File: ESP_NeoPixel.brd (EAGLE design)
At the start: 25.6 x 34.1 mm, 19 parts, among them J1 CONN_08, J2 CONN_08, J3 MKDS3-2-5.00, J4 MKDS3-3-5.00, Q1 BSN20,215, U1 LMZ21700

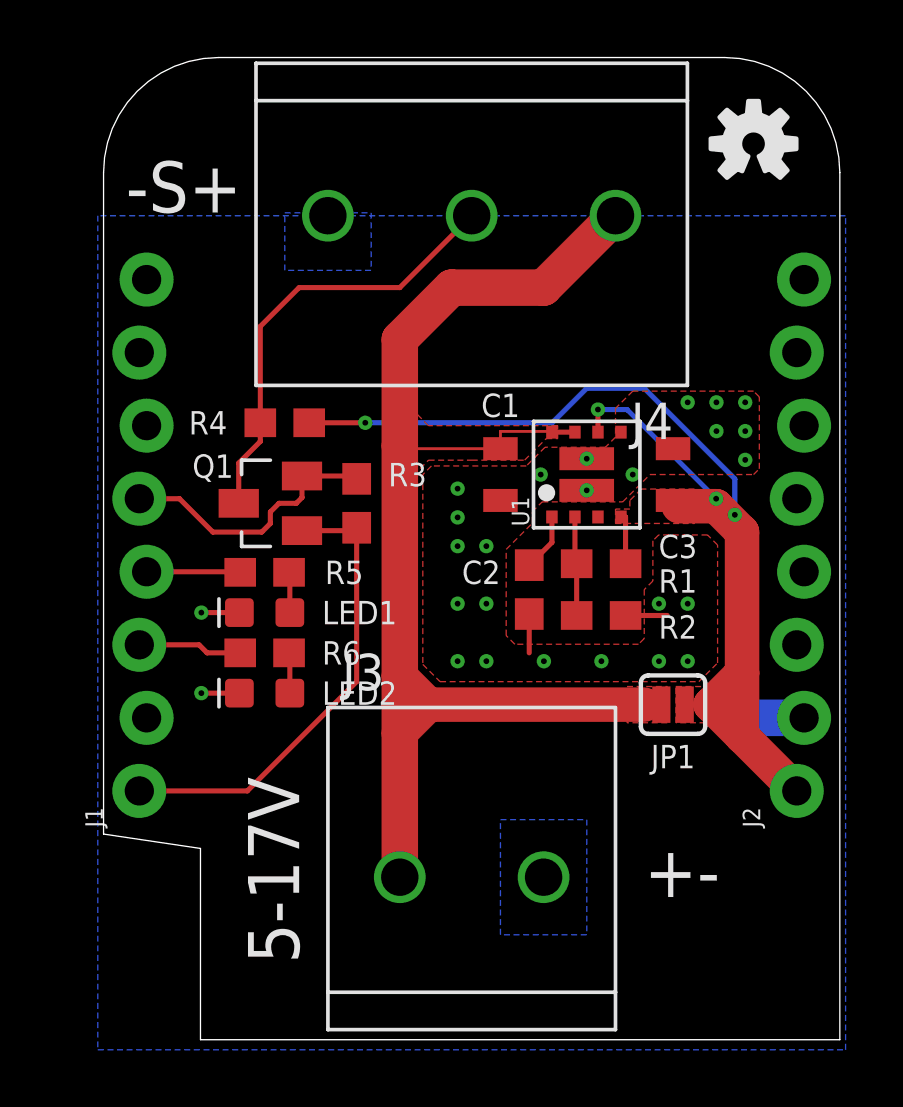
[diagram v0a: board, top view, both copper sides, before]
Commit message: added switch to D8
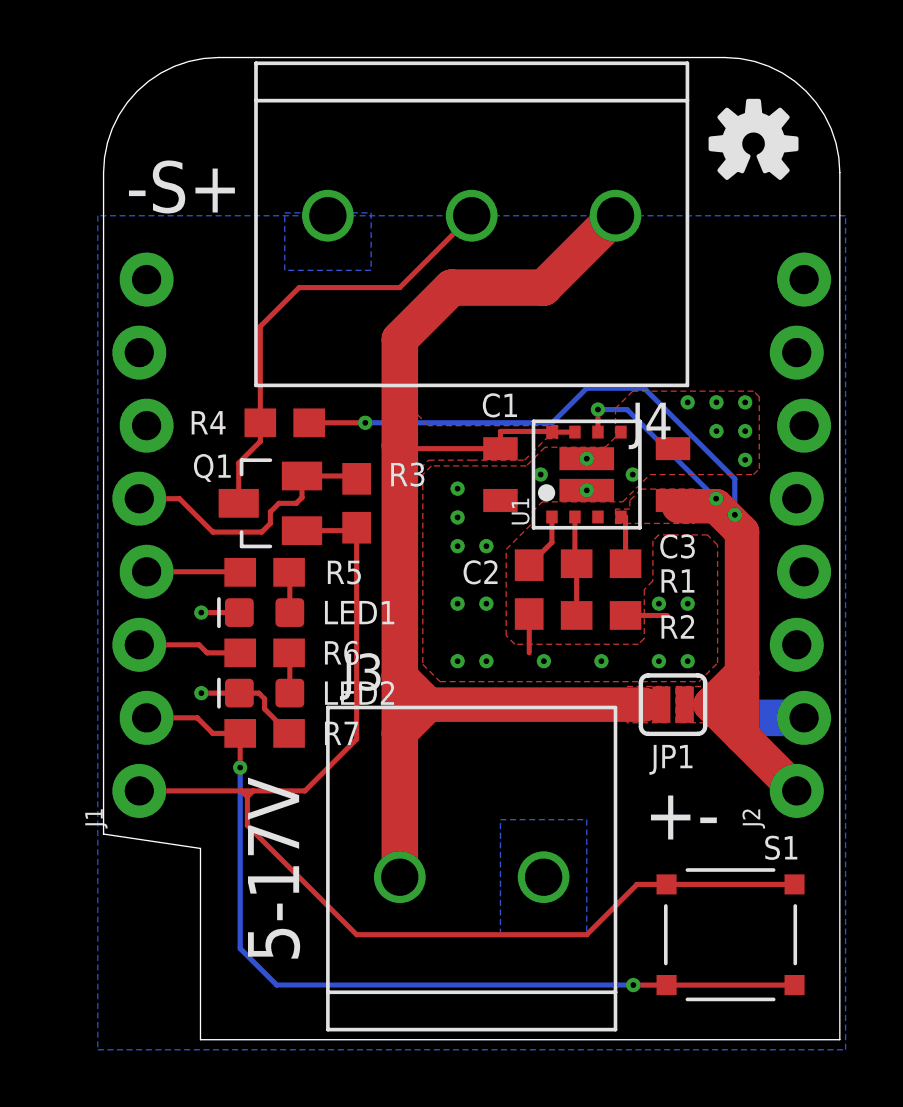
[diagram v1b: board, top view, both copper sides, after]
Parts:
- added R7: 4.7k, SparkFun-Resistors:0603
- added S1: TL3315NF100Q, jonas-switch:TL3315NF100Q
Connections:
- net +3V3: now also S1.P3, S1.P4
- net D8: now also R7.2, S1.P1, S1.P2
- net GND: now also R7.1
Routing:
- net D8: track 0.00 -> 30.8 mm, vias 0 -> 2
- net +3V3: track 16.4 -> 40.5 mm
- net GND: track 7.16 -> 9.67 mm
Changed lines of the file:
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@@
 <layer number="25" name="tNames" color="7" fill="1" visible="yes" active="yes"/>
 <layer number="26" name="bNames" color="7" fill="1" visible="yes" active="yes"/>
-<layer number="27" name="tValues" color="7" fill="1" visible="yes" active="yes"/>
+<layer number="27" name="tValues" color="7" fill="1" visible="no" active="yes"/>
 <layer number="28" name="bValues" color="7" fill="1" visible="no" active="yes"/>
 <layer number="29" name="tStop" color="7" fill="3" visible="no" active="yes"/>
@@
 <wire x1="8.8" y1="25.5" x2="12.8" y2="21.5" width="0" layer="20" curve="-90"/>
 <text x="-6" y="-6" size="1.778" layer="21" rot="R90">5-17V</text>
-<text x="6" y="-2.8" size="1.778" layer="21" align="center-left">+-</text>
+<text x="6" y="-0.8" size="1.778" layer="21" align="center-left">+-</text>
 <text x="-8" y="21" size="1.778" layer="21" rot="R180" align="center-left">-S+</text>
 <text x="0" y="17" size="2.54" layer="22" rot="MR0" align="center">+ S -</text>
@@
 <param name="mdDrill" value="0.21mm"/>
 <param name="mdSmdStop" value="0mil"/>
-<param name="msWidth" value="0.1mm"/>
+<param name="msWidth" value="7mil"/>
 <param name="msDrill" value="0.2mm"/>
 <param name="msMicroVia" value="0.1mm"/>
@@
 <element name="JP1" library="SparkFun-Jumpers" library_urn="urn:adsk.eagle:library:528" package="SMT-JUMPER_2_NO_SILK" package3d_urn="urn:adsk.eagle:package:39279/1" value="JUMPER-SMT_2_NO_SILK" x="7" y="3">
 <attribute name="NAME" x="7" y="1.6" size="0.8128" layer="25" font="vector" align="top-center"/>
-<attribute name="VALUE" x="7" y="1.857" size="0.6096" layer="27" font="vector" ratio="20" align="top-center"/>
 </element>
 <element name="U1" library="jonas_ti" library_urn="urn:adsk.eagle:library:539711" package="SIL0008E" value="LMZ21700" x="4" y="11" rot="R90"/>
@@
 <attribute name="PROD_ID" value=" " x="-7.2" y="4.8" size="1.778" layer="27" rot="R180" display="off"/>
 <attribute name="VALUE" value=" " x="-1.565" y="6.705" size="1.27" layer="27" rot="R180"/>
+</element>
+<element name="S1" library="jonas-switch" package="TL3315NF100Q" value="TL3315NF100Q" x="9" y="-5" rot="R180"/>
+<element name="R7" library="SparkFun-Resistors" library_urn="urn:adsk.eagle:library:532" package="0603" package3d_urn="urn:adsk.eagle:package:39650/1" value="4.7k" x="-7.2" y="2" rot="R180">
+<attribute name="NAME" x="-5.2" y="2" size="0.8128" layer="25" font="vector" rot="R180" align="center-right"/>
+<attribute name="PROD_ID" value=" " x="-7.2" y="2" size="1.778" layer="27" rot="R180" display="off"/>
+<attribute name="VALUE" x="-7.2" y="2.762" size="0.6096" layer="27" font="vector" ratio="20" rot="R180" align="top-center"/>
 </element>
 </elements>
@@
 <signal name="D8">
 <contactref element="J1" pad="2"/>
+<contactref element="S1" pad="P1" route="any" routetag="G$1.P"/>
+<contactref element="S1" pad="P2" route="any" routetag="G$1.P"/>
+<contactref element="R7" pad="2"/>
+<wire x1="-11.303" y1="2.54" x2="-9.54" y2="2.54" width="0.1778" layer="1"/>
+<wire x1="-9.54" y1="2.54" x2="-9" y2="2" width="0.1778" layer="1"/>
+<wire x1="-9" y1="2" x2="-8.05" y2="2" width="0.1778" layer="1"/>
+<wire x1="-8.05" y1="2" x2="-8.05" y2="0.81" width="0.1778" layer="1"/>
+<via x="-8.05" y="0.81" extent="1-16" drill="0.2"/>
+<wire x1="-8.05" y1="0.81" x2="-8.05" y2="-5.48" width="0.1778" layer="16"/>
+<wire x1="-8.05" y1="-5.48" x2="-6.78" y2="-6.75" width="0.1778" layer="16"/>
+<wire x1="-6.78" y1="-6.75" x2="5.62" y2="-6.75" width="0.1778" layer="16"/>
+<via x="5.62" y="-6.75" extent="1-16" drill="0.2"/>
+<wire x1="5.62" y1="-6.75" x2="6.775" y2="-6.75" width="0.1778" layer="1"/>
+<wire x1="11.225" y1="-6.75" x2="6.775" y2="-6.75" width="0.1778" layer="1"/>
 </signal>
 <signal name="D0">
@@
 <wire x1="-8.077" y1="3.4" x2="-9.4" y2="3.4" width="0.1778" layer="1"/>
 <via x="-9.4" y="3.4" extent="1-16" drill="0.2"/>
+<contactref element="R7" pad="1"/>
+<wire x1="-6.35" y1="2" x2="-7.2" y2="2.85" width="0.1778" layer="1"/>
+<wire x1="-7.2" y1="3.2" x2="-7.4" y2="3.4" width="0.1778" layer="1"/>
+<wire x1="-7.4" y1="3.4" x2="-8.077" y2="3.4" width="0.1778" layer="1"/>
+<wire x1="-7.2" y1="2.85" x2="-7.2" y2="3.2" width="0.1778" layer="1"/>
 </signal>
 <signal name="+3V3">
@@
 <wire x1="-5.9" y1="9.05" x2="-4.1" y2="9.05" width="0.1778" layer="1"/>
 <wire x1="-4.1" y1="9.05" x2="-4" y2="9.15" width="0.1778" layer="1"/>
-<wire x1="-11.557" y1="0" x2="-7.8" y2="0" width="0.1778" layer="1"/>
-<wire x1="-4" y1="3.8" x2="-4" y2="9.15" width="0.1778" layer="1"/>
-<wire x1="-7.8" y1="0" x2="-4" y2="3.8" width="0.1778" layer="1"/>
+<wire x1="-8" y1="0" x2="-11.557" y2="0" width="0.1778" layer="1"/>
+<wire x1="-4" y1="9.15" x2="-4" y2="1.8" width="0.1778" layer="1"/>
+<wire x1="-4" y1="1.8" x2="-5.8" y2="0" width="0.1778" layer="1"/>
+<contactref element="S1" pad="P4" route="any" routetag="G$1.S"/>
+<contactref element="S1" pad="P3" route="any" routetag="G$1.S"/>
+<wire x1="6.775" y1="-3.25" x2="5.75" y2="-3.25" width="0.1778" layer="1"/>
+<wire x1="-7.8" y1="-0.2" x2="-7.8" y2="-1.2" width="0.1778" layer="1"/>
+<wire x1="5.75" y1="-3.25" x2="4" y2="-5" width="0.1778" layer="1"/>
+<wire x1="4" y1="-5" x2="-4" y2="-5" width="0.1778" layer="1"/>
+<wire x1="-4" y1="-5" x2="-7.8" y2="-1.2" width="0.1778" layer="1"/>
+<wire x1="-5.8" y1="0" x2="-7.6" y2="0" width="0.1778" layer="1"/>
+<wire x1="-7.6" y1="0" x2="-7.8" y2="-0.2" width="0.1778" layer="1"/>
+<wire x1="-7.8" y1="-0.2" x2="-8" y2="0" width="0.1778" layer="1"/>
+<wire x1="-8" y1="0" x2="-7.6" y2="0" width="0.1778" layer="1"/>
+<wire x1="11.225" y1="-3.25" x2="6.775" y2="-3.25" width="0.1778" layer="1"/>
 </signal>
 <signal name="VCC">
@@
 </polygon>
 <wire x1="-2.5" y1="12" x2="-2.5" y2="15.7" width="1.27" layer="1"/>
-<wire x1="2.79" y1="12.475" x2="2.765" y2="12.5" width="0.1" layer="1"/>
-<wire x1="2.765" y1="12.5" x2="1" y2="12.5" width="0.1" layer="1"/>
-<wire x1="1" y1="12.5" x2="1" y2="11.9" width="0.1" layer="1"/>
-<wire x1="1" y1="11.9" x2="-2.4" y2="11.9" width="0.1" layer="1"/>
-<wire x1="-2.4" y1="11.9" x2="-2.5" y2="12" width="0.1" layer="1"/>
+<wire x1="2.79" y1="12.475" x2="2.765" y2="12.5" width="0.1778" layer="1"/>
+<wire x1="2.765" y1="12.5" x2="1" y2="12.5" width="0.1778" layer="1"/>
+<wire x1="1" y1="12.5" x2="1" y2="11.9" width="0.1778" layer="1"/>
+<wire x1="1" y1="11.9" x2="-2.4" y2="11.9" width="0.1778" layer="1"/>
+<wire x1="-2.4" y1="11.9" x2="-2.5" y2="12" width="0.1778" layer="1"/>
 <wire x1="-1.5" y1="3" x2="6" y2="3" width="1.2" layer="1"/>
 <wire x1="6" y1="3" x2="6.5936" y2="3" width="0.254" layer="1"/>
